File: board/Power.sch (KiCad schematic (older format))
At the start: 6 parts, among them U3 L78L05_TO92

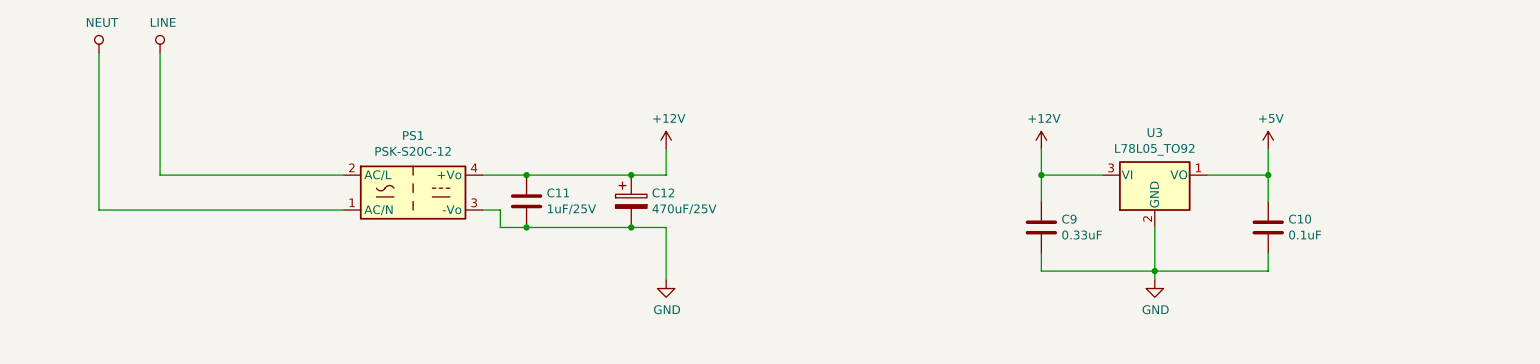
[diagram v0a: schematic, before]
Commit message: Add button 2, LEDs, TVS diode
* Add button 2; rewire to match the prototype
* Add a TVS diode across the 12V rail; value TBD
* Rework power nets into the power sheet; don't use the globals
  inside the sheet, expose the rails as pins.
* Move power protection inside the power sheet.
* Add power LEDs
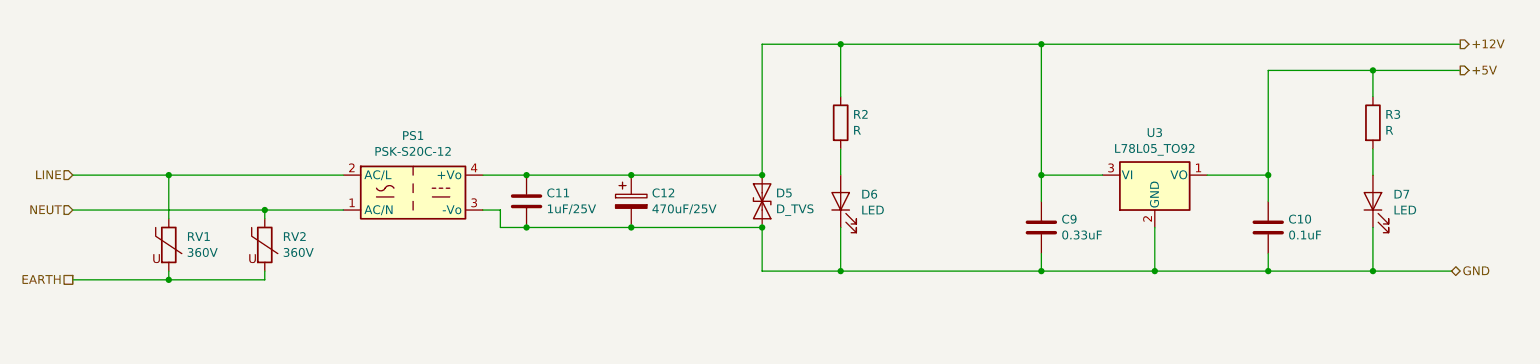
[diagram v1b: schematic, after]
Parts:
- added D5: D_TVS, Diodes_THT:D_DO-41_SOD81_P10.16mm_Horizontal, symbol Device:D_TVS
- added D6, D7: LED, LEDs:LED_D5.0mm, symbol Device:LED
- added R2, R3: R, Resistors_THT:R_Axial_DIN0207_L6.3mm_D2.5mm_P10.16mm_Horizontal, symbol Device:R
- added RV1, RV2: 360V, Varistors:RV_Disc_D15.5_W7.2_P7.5, symbol Device:Varistor
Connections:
- net +12V: now also D5.1 (A1), R2.1
- net +5V: now also R3.1
- net GND: now also D5.2 (A2), D6.1 (K), D7.1 (K)
- net LINE: now also RV1.1
- net NEUT: now also RV2.1
- new net: D6.2 (A), R2.2
- new net: D7.2 (A), R3.2
- new net EARTH: RV1.2, RV2.2
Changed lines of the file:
@@
 Sheet 4 4
 Title "Projector Screen Controller"
-Date ""
+Date "2019-08-31"
 Rev "0.1"
 Comp "Chris Luke"
-Comment1 ""
+Comment1 "https://github.com/flirbleoss/projector-screen-controller"
 Comment2 ""
 Comment3 ""
@@
 	1    0    0    -1
 $EndComp
-$Comp
-L power:GND #PWR011
-U 1 1 5D6F1CC2
-P 7900 3850
-F 0 "#PWR011" H 7900 3600 50  0001 C CNN
-F 1 "GND" H 7905 3677 50  0000 C CNN
-F 2 "" H 7900 3850 50  0001 C CNN
-F 3 "" H 7900 3850 50  0001 C CNN
-	1    7900 3850
-	1    0    0    -1
-$EndComp
 Wire Wire Line
 	7900 3550 7900 3800
-$Comp
-L power:+5V #PWR012
-U 1 1 5D6F2364
-P 8550 3100
-F 0 "#PWR012" H 8550 2950 50  0001 C CNN
-F 1 "+5V" H 8565 3273 50  0000 C CNN
-F 2 "" H 8550 3100 50  0001 C CNN
-F 3 "" H 8550 3100 50  0001 C CNN
-	1    8550 3100
-	1    0    0    -1
-$EndComp
-$Comp
-L power:+12V #PWR010
-U 1 1 5D6F247A
-P 7250 3100
-F 0 "#PWR010" H 7250 2950 50  0001 C CNN
-F 1 "+12V" H 7265 3273 50  0000 C CNN
-F 2 "" H 7250 3100 50  0001 C CNN
-F 3 "" H 7250 3100 50  0001 C CNN
-	1    7250 3100
-	1    0    0    -1
-$EndComp
-Wire Wire Line
-	8550 3100 8550 3250
 Wire Wire Line
 	8550 3250 8200 3250
-Wire Wire Line
-	7250 3100 7250 3250
 Wire Wire Line
 	7250 3250 7600 3250
@@
 Connection ~ 7900 3800
 Wire Wire Line
-	7900 3800 7900 3850
-Wire Wire Line
 	7900 3800 7250 3800
 Wire Wire Line
@@
 	8550 3250 8550 3400
 Connection ~ 8550 3250
-$Comp
-L power:LINE #PWR0104
-U 1 1 5D6F8ADF
-P 2200 2550
-F 0 "#PWR0104" H 2200 2400 50  0001 C CNN
-F 1 "LINE" H 2217 2723 50  0000 C CNN
-F 2 "" H 2200 2550 50  0001 C CNN
-F 3 "" H 2200 2550 50  0001 C CNN
-	1    2200 2550
-	1    0    0    -1
-$EndComp
-$Comp
-L power:NEUT #PWR0105
-U 1 1 5D6F926D
-P 1850 2550
-F 0 "#PWR0105" H 1850 2400 50  0001 C CNN
-F 1 "NEUT" H 1867 2723 50  0000 C CNN
-F 2 "" H 1850 2550 50  0001 C CNN
-F 3 "" H 1850 2550 50  0001 C CNN
-	1    1850 2550
-	1    0    0    -1
-$EndComp
 $Comp
 L Chris_Power:PSK-S20C-12 PS1
@@
 $EndComp
 $Comp
-L power:GND #PWR017
-U 1 1 5D77AE6B
-P 5100 3850
-F 0 "#PWR017" H 5100 3600 50  0001 C CNN
-F 1 "GND" H 5105 3677 50  0000 C CNN
-F 2 "" H 5100 3850 50  0001 C CNN
-F 3 "" H 5100 3850 50  0001 C CNN
-	1    5100 3850
-	1    0    0    -1
-$EndComp
-$Comp
 L Device:C C11
 U 1 1 5D77B64E
@@
 Wire Wire Line
 	4150 3550 4300 3550
-Wire Wire Line
-	2200 2550 2200 3250
-Wire Wire Line
-	2200 3250 3250 3250
-Wire Wire Line
-	1850 2550 1850 3450
-Wire Wire Line
-	1850 3450 3250 3450
-Wire Wire Line
-	5100 3550 5100 3850
-$Comp
-L power:+12V #PWR015
-U 1 1 5D77DEEE
-P 5100 3100
-F 0 "#PWR015" H 5100 2950 50  0001 C CNN
-F 1 "+12V" H 5115 3273 50  0000 C CNN
-F 2 "" H 5100 3100 50  0001 C CNN
-F 3 "" H 5100 3100 50  0001 C CNN
-	1    5100 3100
-	1    0    0    -1
-$EndComp
-Wire Wire Line
-	5100 3250 5100 3100
 $Comp
 L Device:CP C12
@@
 Connection ~ 4300 3550
 Connection ~ 4900 3250
-Wire Wire Line
-	4900 3250 5100 3250
 Connection ~ 4900 3550
 Wire Wire Line
-	4900 3550 5100 3550
-Wire Wire Line
 	4300 3550 4900 3550
 Wire Wire Line
 	4300 3250 4900 3250
+Text HLabel 1700 3250 0    50   Input ~ 0
+LINE
+Text HLabel 1700 3450 0    50   Input ~ 0
+NEUT
+Wire Wire Line
+	1700 3250 2250 3250
+Wire Wire Line
+	1700 3450 2800 3450
+Text HLabel 9650 2500 2    50   Output ~ 0
++12V
+Wire Wire Line
+	7250 2500 7250 3250
+Connection ~ 7250 2500
+Wire Wire Line
+	7250 2500 9650 2500
+Text HLabel 9650 2650 2    50   Output ~ 0
++5V
+Wire Wire Line
+	8550 2650 9150 2650
+Wire Wire Line
+	8550 2650 8550 3250
+Text HLabel 9600 3800 2    50   BiDi ~ 0
+GND
+Wire Wire Line
+	8550 3800 9150 3800
+Connection ~ 8550 3800
+Wire Wire Line
+	7250 3800 6100 3800
+Connection ~ 7250 3800
+$Comp
+L Device:Varistor RV?
+U 1 1 5D700221
+P 2250 3650
+AR Path="/5D700221" Ref="RV?"  Part="1"
+AR Path="/5D68B9FF/5D700221" Ref="RV1"  Part="1"
+F 0 "RV1" H 2353 3696 50  0000 L CNN
+F 1 "360V" H 2353 3605 50  0000 L CNN
+F 2 "Varistors:RV_Disc_D15.5_W7.2_P7.5" V 2180 3650 50  0001 C CNN
+F 3 "~" H 2250 3650 50  0001 C CNN
+F 4 "Vishay" H 2250 3650 50  0001 C CNN "mfr"
+F 5 "VDRS14T230BSE" H 2250 3650 50  0001 C CNN "part#"
+	1    2250 3650
+	1    0    0    -1
+$EndComp
+$Comp
+L Device:Varistor RV?
+U 1 1 5D700227
+P 2800 3650
+AR Path="/5D700227" Ref="RV?"  Part="1"
+AR Path="/5D68B9FF/5D700227" Ref="RV2"  Part="1"
+F 0 "RV2" H 2903 3696 50  0000 L CNN
+F 1 "360V" H 2903 3605 50  0000 L CNN
+F 2 "Varistors:RV_Disc_D15.5_W7.2_P7.5" V 2730 3650 50  0001 C CNN
+F 3 "~" H 2800 3650 50  0001 C CNN
+F 4 "VDRS14T230BSE" H 2800 3650 50  0001 C CNN "part#"
+	1    2800 3650
+	1    0    0    -1
+$EndComp
+Wire Wire Line
+	2250 3800 2250 3850
+Wire Wire Line
+	2800 3800 2800 3850
+Wire Wire Line
+	2800 3850 2250 3850
+Connection ~ 2250 3850
+Text HLabel 1700 3850 0    50   UnSpc ~ 0
+EARTH
+Wire Wire Line
+	1700 3850 2250 3850
+Wire Wire Line
+	2250 3500 2250 3250
+Connection ~ 2250 3250
+Wire Wire Line
+	2250 3250 3250 3250
+Wire Wire Line
+	2800 3500 2800 3450
+Connection ~ 2800 3450
+Wire Wire Line
+	2800 3450 3250 3450
+$Comp
+L Device:D_TVS D5
+U 1 1 5D7077D8
+P 5650 3400
+F 0 "D5" V 5604 3479 50  0000 L CNN
+F 1 "D_TVS" V 5695 3479 50  0000 L CNN
+F 2 "Diodes_THT:D_DO-41_SOD81_P10.16mm_Horizontal" H 5650 3400 50  0001 C CNN
+F 3 "~" H 5650 3400 50  0001 C CNN
+	1    5650 3400
+	0    1    1    0
+$EndComp
+Wire Wire Line
+	5650 3550 5650 3800
+Connection ~ 5650 3550
+Wire Wire Line
+	4900 3550 5650 3550
+Wire Wire Line
+	5650 3250 5650 2500
+Connection ~ 5650 3250
+Wire Wire Line
+	5650 2500 6100 2500
+Wire Wire Line
+	4900 3250 5650 3250
+$Comp
+L Device:LED D6
+U 1 1 5D70BFF3
+P 6100 3400
+F 0 "D6" V 6139 3283 50  0000 R CNN
+F 1 "LED" V 6048 3283 50  0000 R CNN
+F 2 "LEDs:LED_D5.0mm" H 6100 3400 50  0001 C CNN
+F 3 "~" H 6100 3400 50  0001 C CNN
+	1    6100 3400
+	0    -1   -1   0
+$EndComp
+Wire Wire Line
+	6100 3550 6100 3800
+Connection ~ 6100 3800
+Wire Wire Line
+	6100 3800 5650 3800
+$Comp
+L Device:R R2
+U 1 1 5D70D964
+P 6100 2950
+F 0 "R2" H 6170 2996 50  0000 L CNN
+F 1 "R" H 6170 2905 50  0000 L CNN
+F 2 "Resistors_THT:R_Axial_DIN0207_L6.3mm_D2.5mm_P10.16mm_Horizontal" V 6030 2950 50  0001 C CNN
+F 3 "~" H 6100 2950 50  0001 C CNN
+	1    6100 2950
+	1    0    0    -1
+$EndComp
+Wire Wire Line
+	6100 2800 6100 2500
+Connection ~ 6100 2500
+Wire Wire Line
+	6100 2500 7250 2500
+Wire Wire Line
+	6100 3100 6100 3250
+$Comp
+L Device:LED D7
+U 1 1 5D70F3A3
+P 9150 3400
+F 0 "D7" V 9189 3283 50  0000 R CNN
+F 1 "LED" V 9098 3283 50  0000 R CNN
+F 2 "LEDs:LED_D5.0mm" H 9150 3400 50  0001 C CNN
+F 3 "~" H 9150 3400 50  0001 C CNN
+	1    9150 3400
+	0    -1   -1   0
+$EndComp
+Wire Wire Line
+	9150 3550 9150 3800
+Connection ~ 9150 3800
+Wire Wire Line
+	9150 3800 9600 3800
+$Comp
+L Device:R R3
+U 1 1 5D710E5B
+P 9150 2950
+F 0 "R3" H 9220 2996 50  0000 L CNN
+F 1 "R" H 9220 2905 50  0000 L CNN
+F 2 "Resistors_THT:R_Axial_DIN0207_L6.3mm_D2.5mm_P10.16mm_Horizontal" V 9080 2950 50  0001 C CNN
+F 3 "~" H 9150 2950 50  0001 C CNN
+	1    9150 2950
+	1    0    0    -1
+$EndComp
+Wire Wire Line
+	9150 3100 9150 3250
+Wire Wire Line
+	9150 2800 9150 2650
+Connection ~ 9150 2650
+Wire Wire Line
+	9150 2650 9650 2650
 $EndSCHEMATC

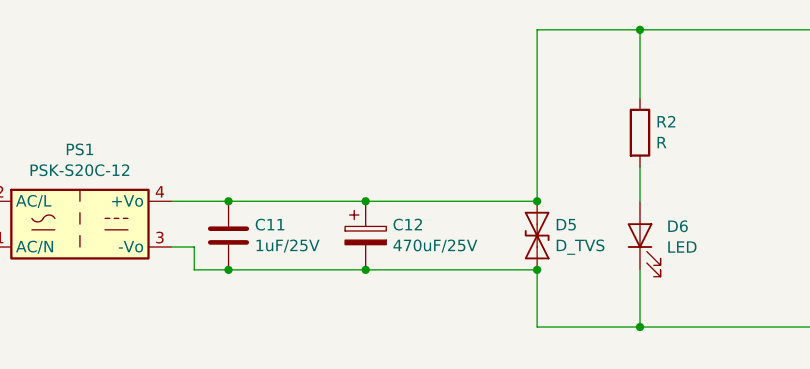
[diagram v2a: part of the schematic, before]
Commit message: Update fuse footprint, add more 3d models, update TODO
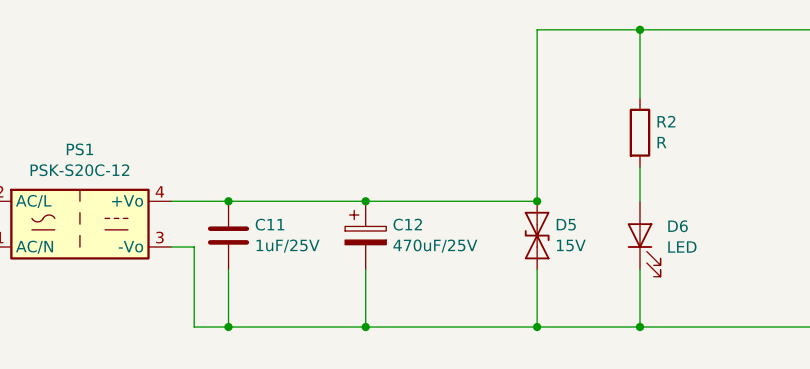
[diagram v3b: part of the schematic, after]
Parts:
- C12: footprint Capacitors_THT:CP_Radial_D10.0mm_P2.50mm -> Capacitors_THT:CP_Radial_D10.0mm_P2.50mm_P5.00mm
- D5: value D_TVS -> 15V; mfr (none) -> Vishay; part# (none) -> 1.5KE15CA-E3/54
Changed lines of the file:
@@
 Wire Wire Line
 	4050 3450 4150 3450
-Wire Wire Line
-	4150 3450 4150 3550
-Wire Wire Line
-	4150 3550 4300 3550
 $Comp
 L Device:CP C12
@@
 F 0 "C12" H 5018 3446 50  0000 L CNN
 F 1 "470uF/25V" H 5018 3355 50  0000 L CNN
-F 2 "Capacitors_THT:CP_Radial_D10.0mm_P2.50mm" H 4938 3250 50  0001 C CNN
+F 2 "Capacitors_THT:CP_Radial_D10.0mm_P2.50mm_P5.00mm" H 4938 3250 50  0001 C CNN
 F 3 "~" H 4900 3400 50  0001 C CNN
 	1    4900 3400
@@
 $EndComp
 Connection ~ 4300 3250
-Connection ~ 4300 3550
 Connection ~ 4900 3250
-Connection ~ 4900 3550
-Wire Wire Line
-	4300 3550 4900 3550
 Wire Wire Line
 	4300 3250 4900 3250
@@
 P 5650 3400
 F 0 "D5" V 5604 3479 50  0000 L CNN
-F 1 "D_TVS" V 5695 3479 50  0000 L CNN
+F 1 "15V" V 5695 3479 50  0000 L CNN
 F 2 "Diodes_THT:D_DO-41_SOD81_P10.16mm_Horizontal" H 5650 3400 50  0001 C CNN
-F 3 "~" H 5650 3400 50  0001 C CNN
+F 3 "https://www.mouser.com/datasheet/2/427/15ke-240293.pdf" H 5650 3400 50  0001 C CNN
+F 4 "Vishay" H 5650 3400 50  0001 C CNN "mfr"
+F 5 "1.5KE15CA-E3/54" H 5650 3400 50  0001 C CNN "part#"
 	1    5650 3400
 	0    1    1    0
@@
 Wire Wire Line
 	5650 3550 5650 3800
-Connection ~ 5650 3550
-Wire Wire Line
-	4900 3550 5650 3550
 Wire Wire Line
 	5650 3250 5650 2500
@@
 Wire Wire Line
 	9150 2650 9650 2650
+Wire Wire Line
+	4150 3800 4300 3800
+Connection ~ 5650 3800
+Wire Wire Line
+	4900 3550 4900 3800
+Connection ~ 4900 3800
+Wire Wire Line
+	4900 3800 5650 3800
+Wire Wire Line
+	4300 3550 4300 3800
+Connection ~ 4300 3800
+Wire Wire Line
+	4300 3800 4900 3800
+Wire Wire Line
+	4150 3450 4150 3800
 $EndSCHEMATC

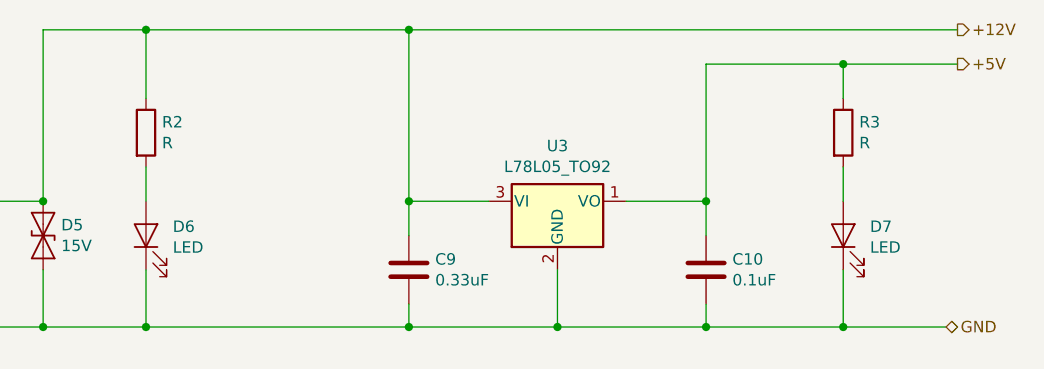
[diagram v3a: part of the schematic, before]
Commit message: Add nominal LED R values; ground plane tweaks; first board spin
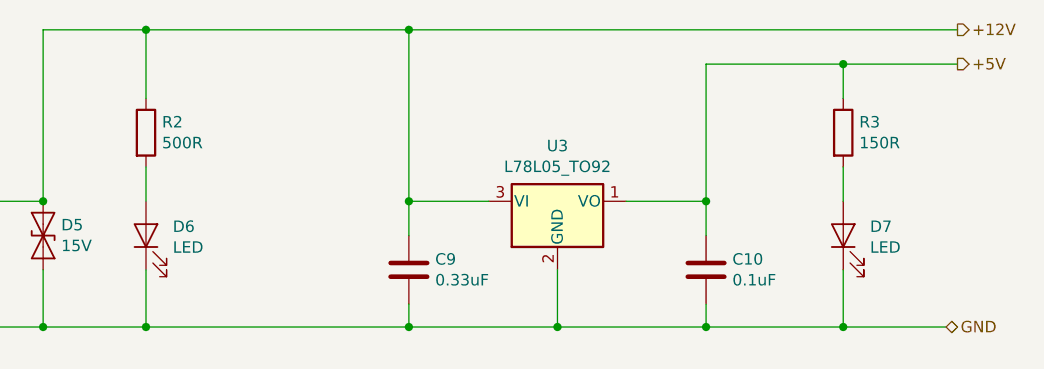
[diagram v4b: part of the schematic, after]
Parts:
- R2: value R -> 500R
- R3: value R -> 150R
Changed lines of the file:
@@
 P 6100 2950
 F 0 "R2" H 6170 2996 50  0000 L CNN
-F 1 "R" H 6170 2905 50  0000 L CNN
+F 1 "500R" H 6170 2905 50  0000 L CNN
 F 2 "Resistors_THT:R_Axial_DIN0207_L6.3mm_D2.5mm_P10.16mm_Horizontal" V 6030 2950 50  0001 C CNN
 F 3 "~" H 6100 2950 50  0001 C CNN
@@
 P 9150 2950
 F 0 "R3" H 9220 2996 50  0000 L CNN
-F 1 "R" H 9220 2905 50  0000 L CNN
+F 1 "150R" H 9220 2905 50  0000 L CNN
 F 2 "Resistors_THT:R_Axial_DIN0207_L6.3mm_D2.5mm_P10.16mm_Horizontal" V 9080 2950 50  0001 C CNN
 F 3 "~" H 9150 2950 50  0001 C CNN

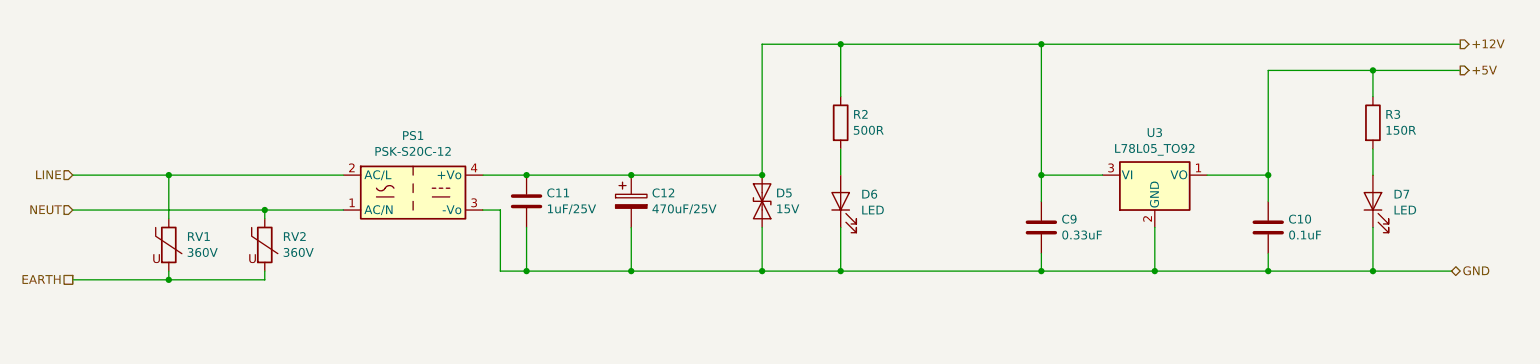
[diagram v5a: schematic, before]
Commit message: Minor layout tweaks, component updates
* Add an MCU driven status LED
* Update LED current limit resistor values
* Minor trace tweaks for clearance
* Based on empirical measurements of rev 0.1 board, adjust the location of the
  board mounting holes.
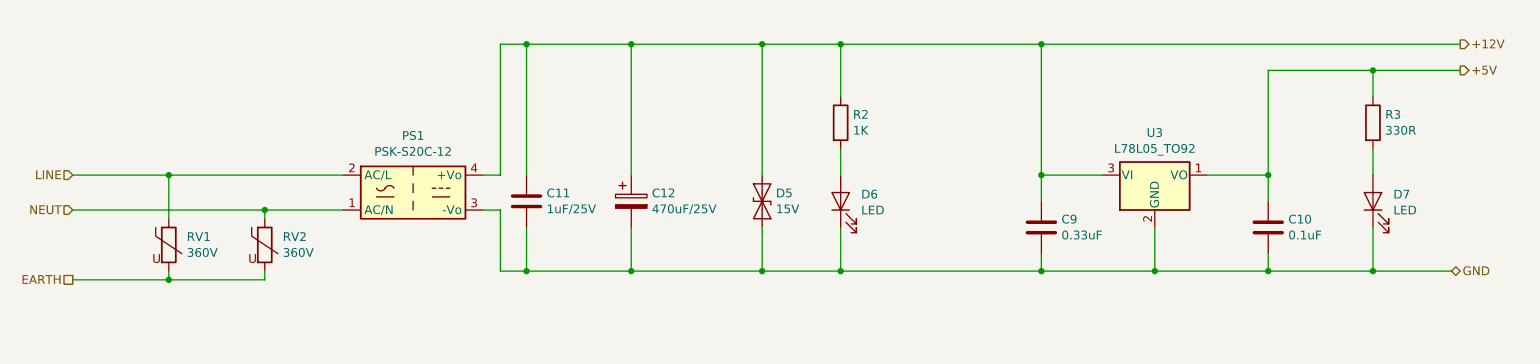
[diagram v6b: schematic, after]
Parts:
- R2: value 500R -> 1K
- R3: value 150R -> 330R
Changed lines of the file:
@@
 $EndComp
-Wire Wire Line
-	4050 3250 4300 3250
 Wire Wire Line
 	4050 3450 4150 3450
@@
 	1    0    0    -1
 $EndComp
-Connection ~ 4300 3250
-Connection ~ 4900 3250
-Wire Wire Line
-	4300 3250 4900 3250
 Text HLabel 1700 3250 0    50   Input ~ 0
 LINE
@@
 Wire Wire Line
 	5650 3250 5650 2500
-Connection ~ 5650 3250
 Wire Wire Line
 	5650 2500 6100 2500
-Wire Wire Line
-	4900 3250 5650 3250
 $Comp
 L Device:LED D6
@@
 P 6100 2950
 F 0 "R2" H 6170 2996 50  0000 L CNN
-F 1 "500R" H 6170 2905 50  0000 L CNN
+F 1 "1K" H 6170 2905 50  0000 L CNN
 F 2 "Resistors_THT:R_Axial_DIN0207_L6.3mm_D2.5mm_P10.16mm_Horizontal" V 6030 2950 50  0001 C CNN
 F 3 "~" H 6100 2950 50  0001 C CNN
@@
 P 9150 2950
 F 0 "R3" H 9220 2996 50  0000 L CNN
-F 1 "150R" H 9220 2905 50  0000 L CNN
+F 1 "330R" H 9220 2905 50  0000 L CNN
 F 2 "Resistors_THT:R_Axial_DIN0207_L6.3mm_D2.5mm_P10.16mm_Horizontal" V 9080 2950 50  0001 C CNN
 F 3 "~" H 9150 2950 50  0001 C CNN
@@
 Wire Wire Line
 	4150 3450 4150 3800
+Wire Wire Line
+	4050 3250 4150 3250
+Wire Wire Line
+	4150 3250 4150 2500
+Wire Wire Line
+	4150 2500 4300 2500
+Connection ~ 5650 2500
+Wire Wire Line
+	4900 3250 4900 2500
+Connection ~ 4900 2500
+Wire Wire Line
+	4900 2500 5650 2500
+Wire Wire Line
+	4300 3250 4300 2500
+Connection ~ 4300 2500
+Wire Wire Line
+	4300 2500 4900 2500
 $EndSCHEMATC
